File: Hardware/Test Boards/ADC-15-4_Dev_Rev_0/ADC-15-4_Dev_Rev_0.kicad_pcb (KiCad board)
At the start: 2 copper layers, 50 x 44.3 mm, 9 parts, among them J1 RF IN, J2 RF THRU IN, J3 RF COUPLED, J4 RF THRU OUT, J5 RF OUT

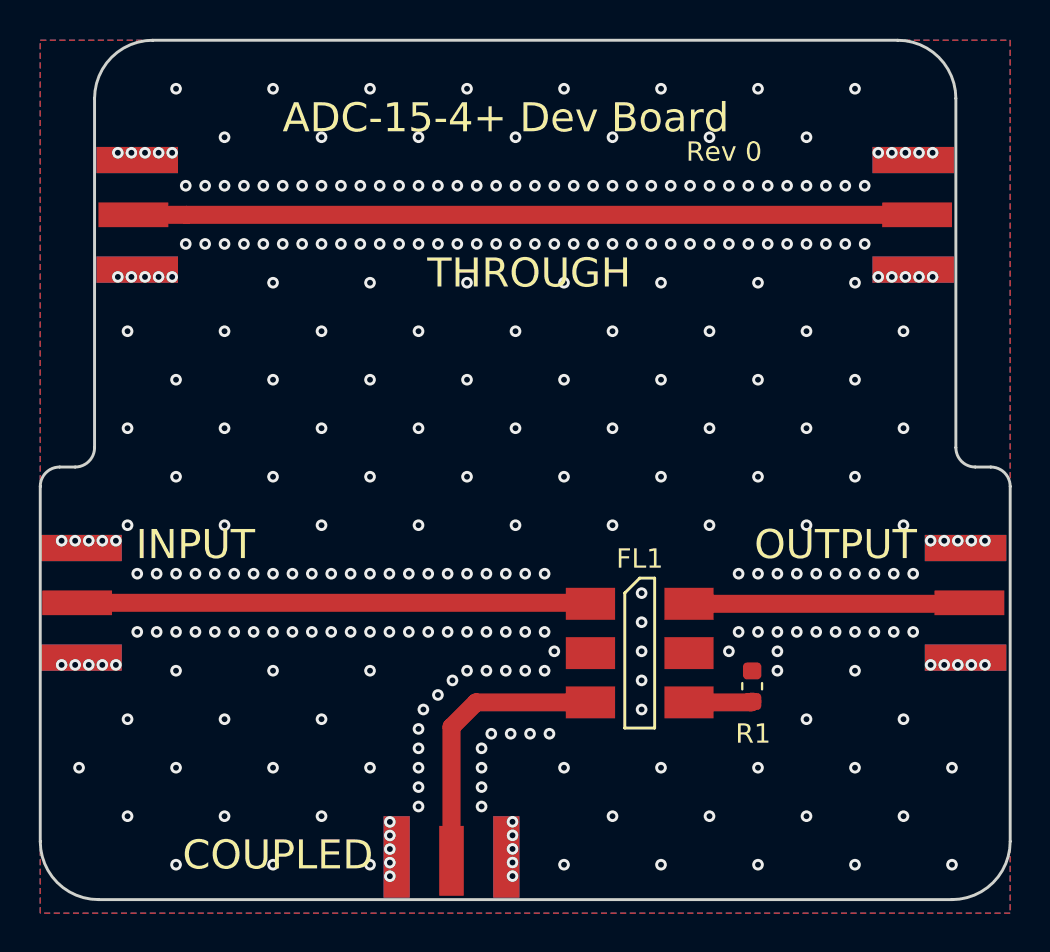
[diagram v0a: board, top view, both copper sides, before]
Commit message: Added FV1206 and DIP switch models and footprints, along with micro USB footprint
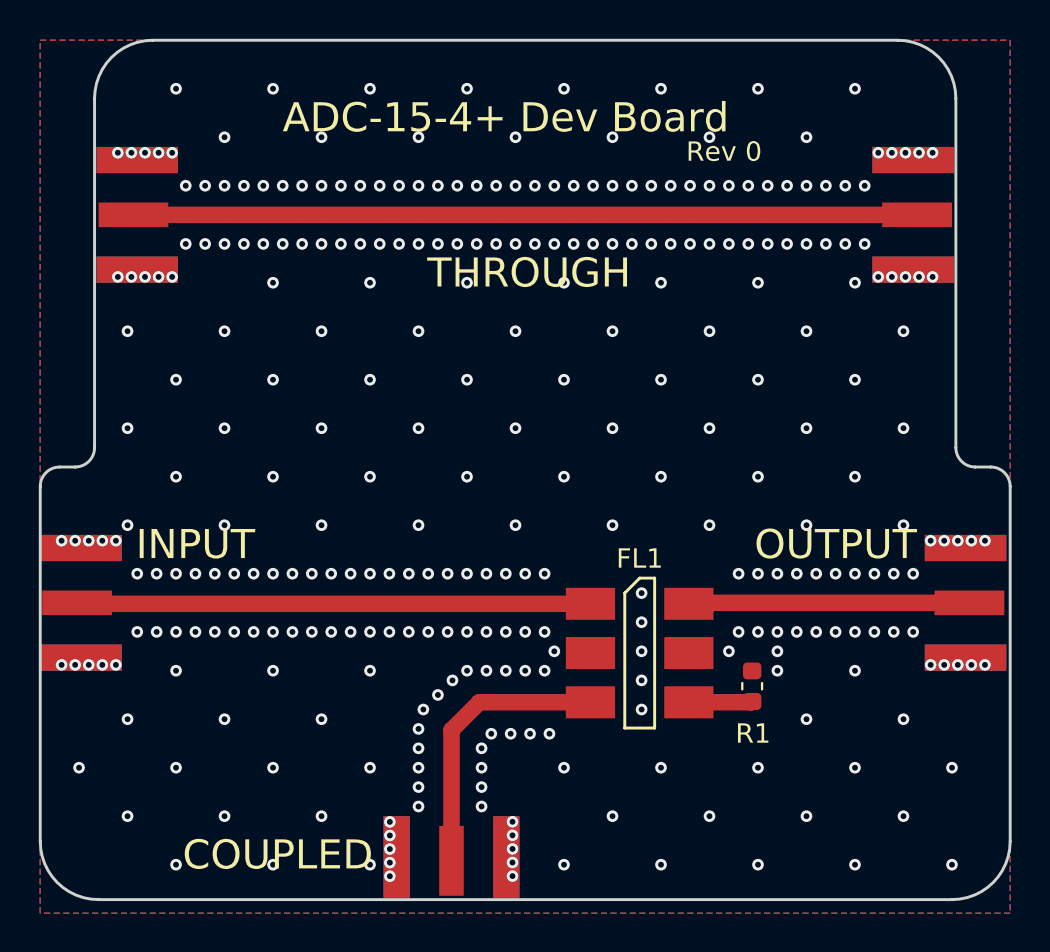
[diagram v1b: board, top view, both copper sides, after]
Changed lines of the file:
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@@
     (thickness 1.6)
     (drawings 22)
-    (tracks 326)
+    (tracks 327)
     (zones 0)
     (modules 9)
@@
   )
   (setup
-    (last_trace_width 0.25)
-    (user_trace_width 0.93)
+    (last_trace_width 0.85)
+    (user_trace_width 0.85)
     (trace_clearance 0.2)
-    (zone_clearance 0.7)
+    (zone_clearance 0.5)
     (zone_45_only no)
     (trace_min 0.2)
@@
     (mod_text_size 1 1)
     (mod_text_width 0.15)
-    (pad_size 0.875 0.95)
+    (pad_size 1.65 2.54)
     (pad_drill 0)
     (pad_to_mask_clearance 0.051)
@@
       (net 5 "Net-(FL1-Pad4)"))
     (pad 2 smd rect (at -2.637222 0.59101 270) (size 1.65 2.54) (layers F.Cu F.Paste F.Mask)
-      (net 4 GND))
+      (net 4 GND) (zone_connect 2))
     (pad 5 smd rect (at 2.442778 0.59101 270) (size 1.65 2.54) (layers F.Cu F.Paste F.Mask)
       (net 3 "Net-(FL1-Pad5)"))
@@
     (fp_line (start -0.8 0.4) (end -0.8 -0.4) (layer F.Fab) (width 0.1))
     (pad 2 smd roundrect (at 0.7875 0 90) (size 0.875 0.95) (layers F.Cu F.Paste F.Mask) (roundrect_rratio 0.25)
-      (net 4 GND))
+      (net 4 GND) (zone_connect 2))
     (pad 1 smd roundrect (at -0.7875 0 90) (size 0.875 0.95) (layers F.Cu F.Paste F.Mask) (roundrect_rratio 0.25)
       (net 5 "Net-(FL1-Pad4)"))
@@
   (gr_line (start 98 78) (end 98 96.3) (layer Edge.Cuts) (width 0.15))
   (segment (start 145.84899 84.05101) (end 145.9 84) (width 0.93) (layer F.Cu) (net 1))
-  (segment (start 131.442778 84.05101) (end 145.84899 84.05101) (width 0.93) (layer F.Cu) (net 1))
+  (segment (start 131.493788 84) (end 131.442778 84.05101) (width 0.85) (layer F.Cu) (net 1))
+  (segment (start 145.9 84) (end 131.493788 84) (width 0.85) (layer F.Cu) (net 1))
   (segment (start 126.311768 84) (end 126.362778 84.05101) (width 0.93) (layer F.Cu) (net 2))
-  (segment (start 99.9 84) (end 126.311768 84) (width 0.93) (layer F.Cu) (net 2))
+  (segment (start 99.95101 84.05101) (end 99.9 84) (width 0.85) (layer F.Cu) (net 2))
+  (segment (start 126.362778 84.05101) (end 99.95101 84.05101) (width 0.85) (layer F.Cu) (net 2))
   (via (at 102 60.8) (size 0.6) (drill 0.3) (layers F.Cu B.Cu) (net 4))
   (via (at 102.7 60.8) (size 0.6) (drill 0.3) (layers F.Cu B.Cu) (net 4))
@@
   (via (at 118.5 88.75) (size 0.6) (drill 0.3) (layers F.Cu B.Cu) (net 4))
   (segment (start 131.473788 89.1) (end 131.442778 89.13101) (width 0.93) (layer F.Cu) (net 5))
-  (segment (start 134.65649 89.13101) (end 134.7 89.0875) (width 0.93) (layer F.Cu) (net 5))
-  (segment (start 131.442778 89.13101) (end 134.65649 89.13101) (width 0.93) (layer F.Cu) (net 5))
-  (segment (start 119.2 90.4) (end 119.2 97.3) (width 0.93) (layer F.Cu) (net 6))
-  (segment (start 120.46899 89.13101) (end 119.2 90.4) (width 0.93) (layer F.Cu) (net 6))
-  (segment (start 120.46899 89.13101) (end 126.362778 89.13101) (width 0.93) (layer F.Cu) (net 6))
-  (segment (start 105.53 64) (end 143.2 64) (width 0.93) (layer F.Cu) (net 7))
-  (segment (start 102.8 64) (end 105.53 64) (width 0.93) (layer F.Cu) (net 7))
+  (segment (start 134.65649 89.13101) (end 134.7 89.0875) (width 0.85) (layer F.Cu) (net 5))
+  (segment (start 131.442778 89.13101) (end 134.65649 89.13101) (width 0.85) (layer F.Cu) (net 5))
+  (segment (start 119.2 90.56202) (end 119.2 97.3) (width 0.85) (layer F.Cu) (net 6))
+  (segment (start 126.362778 89.13101) (end 120.63101 89.13101) (width 0.85) (layer F.Cu) (net 6))
+  (segment (start 120.63101 89.13101) (end 119.2 90.56202) (width 0.85) (layer F.Cu) (net 6))
+  (segment (start 102.8 64) (end 143.2 64) (width 0.85) (layer F.Cu) (net 7))
   (zone (net 4) (net_name GND) (layer F.Cu) (hatch edge 0.508)
-    (connect_pads (clearance 0.7))
+    (connect_pads (clearance 0.5))
     (min_thickness 0.254)
     (fill yes (arc_segments 16) (thermal_gap 0.508) (thermal_bridge_width 0.508))
